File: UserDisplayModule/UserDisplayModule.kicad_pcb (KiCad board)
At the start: 2 copper layers, 0 parts

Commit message: doubled LEDs + started PCB
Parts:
- added C1: 10µ, Capacitor_SMD:C_0805_2012Metric, F.Cu at (60.5, 129.8)
- added D1: MAINS, LED_SMD:LED_0805_2012Metric, F.Cu at (89.2, 78.9)
- added D10: BAT3, LED_SMD:LED_0805_2012Metric, F.Cu at (93.7, 91.1)
- added D11: BAT8, LED_SMD:LED_0805_2012Metric, F.Cu at (100.0, 41.8)
- added D12: BAT1, LED_SMD:LED_0805_2012Metric, F.Cu at (100.0, 44.9)
- added D13: BAT7, LED_SMD:LED_0805_2012Metric, F.Cu at (100.0, 47.9)
- added D14: BAT1, LED_SMD:LED_0805_2012Metric, F.Cu at (100.0, 51.0)
- added D15: BAT6, LED_SMD:LED_0805_2012Metric, F.Cu at (104.5, 41.8)
- added D16: BAT1, LED_SMD:LED_0805_2012Metric, F.Cu at (104.5, 44.9)
- added D17: BAT5, LED_SMD:LED_0805_2012Metric, F.Cu at (104.5, 47.9)
- added D18: BAT1, LED_SMD:LED_0805_2012Metric, F.Cu at (104.5, 51.0)
- added D19: BAT4, LED_SMD:LED_0805_2012Metric, F.Cu at (108.9, 41.8)
- added D2: MAINS, LED_SMD:LED_0805_2012Metric, F.Cu at (89.2, 82.0)
- added D20: BAT1, LED_SMD:LED_0805_2012Metric, F.Cu at (108.9, 44.9)
- added D21: BAT3, LED_SMD:LED_0805_2012Metric, F.Cu at (108.9, 47.9)
- added D22: BAT1, LED_SMD:LED_0805_2012Metric, F.Cu at (108.9, 51.0)
- added D23: BAT2, LED_SMD:LED_0805_2012Metric, F.Cu at (113.4, 41.8)
- added D24: BAT1, LED_SMD:LED_0805_2012Metric, F.Cu at (113.4, 44.9)
- added D25: BAT1, LED_SMD:LED_0805_2012Metric, F.Cu at (113.4, 47.9)
- added D26: BAT1, LED_SMD:LED_0805_2012Metric, F.Cu at (113.4, 51.0)
- added D27: SEG7, LED_SMD:LED_0805_2012Metric, F.Cu at (208.0, 46.4)
- added D28: BAT1, LED_SMD:LED_0805_2012Metric, F.Cu at (208.0, 49.9)
- added D29: SEG6, LED_SMD:LED_0805_2012Metric, F.Cu at (205.1, 52.4)
- added D3: SOLAR, LED_SMD:LED_0805_2012Metric, F.Cu at (89.2, 85.0)
- added D30: BAT1, LED_SMD:LED_0805_2012Metric, F.Cu at (201.6, 52.4)
- added D31: SEG5, LED_SMD:LED_0805_2012Metric, F.Cu at (192.3, 52.4)
- added D32: BAT1, LED_SMD:LED_0805_2012Metric, F.Cu at (195.8, 52.4)
- added D33: SEG4, LED_SMD:LED_0805_2012Metric, F.Cu at (189.5, 46.4)
- added D34: BAT1, LED_SMD:LED_0805_2012Metric, F.Cu at (189.5, 49.9)
- added D35: SEG3, LED_SMD:LED_0805_2012Metric, F.Cu at (195.8, 43.9)
- added D36: BAT1, LED_SMD:LED_0805_2012Metric, F.Cu at (192.3, 43.9)
- added D37: SEG2, LED_SMD:LED_0805_2012Metric, F.Cu at (205.1, 43.9)
- added D38: BAT1, LED_SMD:LED_0805_2012Metric, F.Cu at (201.6, 43.9)
- added D39: SEG1, LED_SMD:LED_0805_2012Metric, F.Cu at (198.8, 46.4)
- added D4: BATTERY, LED_SMD:LED_0805_2012Metric, F.Cu at (89.2, 88.1)
- added D40: BAT1, LED_SMD:LED_0805_2012Metric, F.Cu at (198.8, 49.9)
- added D41: PTVS5V0Z1USK, Diode_SMD:Nexperia_DSN1608-2_1.6x0.8mm, F.Cu at (52.5, 147.3)
- added D42: COL2, LED_SMD:LED_0805_2012Metric, F.Cu at (98.1, 78.9)
- added D43: BAT3, LED_SMD:LED_0805_2012Metric, F.Cu at (98.1, 82.0)
- added D44: COL1, LED_SMD:LED_0805_2012Metric, F.Cu at (98.1, 85.0)
- added D45: BAT3, LED_SMD:LED_0805_2012Metric, F.Cu at (98.1, 88.1)
- added D46: SEG7, LED_SMD:LED_0805_2012Metric, F.Cu at (208.0, 70.2)
- added D47: BAT1, LED_SMD:LED_0805_2012Metric, F.Cu at (208.0, 73.8)
- added D48: SEG6, LED_SMD:LED_0805_2012Metric, F.Cu at (205.1, 76.3)
- added D49: BAT1, LED_SMD:LED_0805_2012Metric, F.Cu at (201.6, 76.3)
- added D5: BATTERY, LED_SMD:LED_0805_2012Metric, F.Cu at (89.2, 91.1)
- added D50: SEG5, LED_SMD:LED_0805_2012Metric, F.Cu at (192.3, 76.2)
- added D51: BAT1, LED_SMD:LED_0805_2012Metric, F.Cu at (195.8, 76.2)
- added D52: SEG4, LED_SMD:LED_0805_2012Metric, F.Cu at (189.5, 70.2)
- added D53: BAT1, LED_SMD:LED_0805_2012Metric, F.Cu at (189.5, 73.7)
- added D54: SEG3, LED_SMD:LED_0805_2012Metric, F.Cu at (195.8, 67.8)
- added D55: BAT1, LED_SMD:LED_0805_2012Metric, F.Cu at (192.3, 67.8)
- added D56: SEG2, LED_SMD:LED_0805_2012Metric, F.Cu at (205.1, 67.8)
- added D57: BAT1, LED_SMD:LED_0805_2012Metric, F.Cu at (201.6, 67.8)
- added D58: SEG1, LED_SMD:LED_0805_2012Metric, F.Cu at (198.8, 70.2)
- added D59: BAT1, LED_SMD:LED_0805_2012Metric, F.Cu at (198.8, 73.8)
- added D6: BAT7, LED_SMD:LED_0805_2012Metric, F.Cu at (93.7, 78.9)
- added D60: SEG7, LED_SMD:LED_0805_2012Metric, F.Cu at (208.0, 94.2)
- added D61: BAT1, LED_SMD:LED_0805_2012Metric, F.Cu at (208.0, 97.8)
- added D62: SEG6, LED_SMD:LED_0805_2012Metric, F.Cu at (205.1, 100.2)
- added D63: BAT1, LED_SMD:LED_0805_2012Metric, F.Cu at (201.6, 100.2)
- added D64: SEG5, LED_SMD:LED_0805_2012Metric, F.Cu at (192.3, 100.2)
- added D65: BAT1, LED_SMD:LED_0805_2012Metric, F.Cu at (195.8, 100.2)
- added D66: SEG4, LED_SMD:LED_0805_2012Metric, F.Cu at (189.5, 94.2)
- added D67: BAT1, LED_SMD:LED_0805_2012Metric, F.Cu at (189.5, 97.8)
- added D68: SEG3, LED_SMD:LED_0805_2012Metric, F.Cu at (195.8, 91.8)
- added D69: BAT1, LED_SMD:LED_0805_2012Metric, F.Cu at (192.3, 91.8)
- added D7: SYS WARN, LED_SMD:LED_0805_2012Metric, F.Cu at (93.7, 82.0)
- added D70: SEG2, LED_SMD:LED_0805_2012Metric, F.Cu at (205.1, 91.8)
- added D71: BAT1, LED_SMD:LED_0805_2012Metric, F.Cu at (201.6, 91.8)
- added D72: SEG1, LED_SMD:LED_0805_2012Metric, F.Cu at (198.8, 94.2)
- added D73: BAT1, LED_SMD:LED_0805_2012Metric, F.Cu at (198.8, 97.8)
- added D74: SEG7, LED_SMD:LED_0805_2012Metric, F.Cu at (207.7, 115.4)
- added D75: BAT1, LED_SMD:LED_0805_2012Metric, F.Cu at (207.7, 118.9)
- added D76: SEG6, LED_SMD:LED_0805_2012Metric, F.Cu at (204.8, 121.5)
- added D77: BAT1, LED_SMD:LED_0805_2012Metric, F.Cu at (201.2, 121.5)
- added D78: SEG5, LED_SMD:LED_0805_2012Metric, F.Cu at (192.0, 121.5)
- added D79: BAT1, LED_SMD:LED_0805_2012Metric, F.Cu at (195.5, 121.5)
- added D8: BAT5, LED_SMD:LED_0805_2012Metric, F.Cu at (93.7, 85.0)
- added D80: SEG4, LED_SMD:LED_0805_2012Metric, F.Cu at (189.2, 115.4)
- added D81: BAT1, LED_SMD:LED_0805_2012Metric, F.Cu at (189.2, 118.9)
- added D82: SEG3, LED_SMD:LED_0805_2012Metric, F.Cu at (195.5, 113.0)
- added D83: BAT1, LED_SMD:LED_0805_2012Metric, F.Cu at (192.0, 113.0)
- added D84: SEG2, LED_SMD:LED_0805_2012Metric, F.Cu at (204.8, 113.0)
- added D85: BAT1, LED_SMD:LED_0805_2012Metric, F.Cu at (201.3, 113.0)
- added D86: SEG1, LED_SMD:LED_0805_2012Metric, F.Cu at (198.4, 115.5)
- added D87: BAT1, LED_SMD:LED_0805_2012Metric, F.Cu at (198.4, 119.0)
- added D9: SYS FAIL, LED_SMD:LED_0805_2012Metric, F.Cu at (93.7, 88.1)
- added H1: MountingHole_Pad, MountingHole:MountingHole_3.2mm_M3_Pad, F.Cu at (32.5, 32.5)
- added H2: MountingHole_Pad, MountingHole:MountingHole_3.2mm_M3_Pad, F.Cu at (32.5, 156.5)
- added H3: MountingHole_Pad, MountingHole:MountingHole_3.2mm_M3_Pad, F.Cu at (220.5, 32.5)
- added H4: MountingHole_Pad, MountingHole:MountingHole_3.2mm_M3_Pad, F.Cu at (220.5, 156.5)
- added J1: RJ45_Shielded, Connector_RJ:RJ45_Shielded_EthernetJack, F.Cu at (48.7, 32.5)
- added R1: R_US, Resistor_SMD:R_0805_2012Metric, F.Cu at (84.8, 78.9)
- added R10: R_US, Resistor_SMD:R_0805_2012Metric, F.Cu at (85.0, 56.6)
- added R11: R_US, Resistor_SMD:R_0805_2012Metric, F.Cu at (85.0, 59.5)
- added R12: R_US, Resistor_SMD:R_0805_2012Metric, F.Cu at (85.0, 62.5)
- added R13: R_US, Resistor_SMD:R_0805_2012Metric, F.Cu at (179.1, 40.1)
- added R14: R_US, Resistor_SMD:R_0805_2012Metric, F.Cu at (179.1, 43.0)
- added R15: R_US, Resistor_SMD:R_0805_2012Metric, F.Cu at (179.1, 46.0)
- added R16: R_US, Resistor_SMD:R_0805_2012Metric, F.Cu at (179.1, 49.0)
- added R17: R_US, Resistor_SMD:R_0805_2012Metric, F.Cu at (179.1, 51.9)
- added R18: R_US, Resistor_SMD:R_0805_2012Metric, F.Cu at (179.1, 54.9)
- added R19: R_US, Resistor_SMD:R_0805_2012Metric, F.Cu at (179.1, 57.8)
- added R2: R_US, Resistor_SMD:R_0805_2012Metric, F.Cu at (84.8, 81.9)
- added R20: R_US, Resistor_SMD:R_0805_2012Metric, F.Cu at (84.8, 90.7)
- added R21: R_US, Resistor_SMD:R_0805_2012Metric, F.Cu at (84.8, 93.7)
- added R22: 16k, Resistor_SMD:R_0805_2012Metric, F.Cu at (56.1, 129.8)
- added R23: R_US, Resistor_SMD:R_0805_2012Metric, F.Cu at (84.8, 96.6)
- added R24: R_US, Resistor_SMD:R_0805_2012Metric, F.Cu at (178.7, 63.6)
- added R25: R_US, Resistor_SMD:R_0805_2012Metric, F.Cu at (178.7, 66.5)
- added R26: R_US, Resistor_SMD:R_0805_2012Metric, F.Cu at (178.7, 69.5)
- added R27: R_US, Resistor_SMD:R_0805_2012Metric, F.Cu at (178.7, 72.4)
- added R28: R_US, Resistor_SMD:R_0805_2012Metric, F.Cu at (178.7, 75.4)
- added R29: R_US, Resistor_SMD:R_0805_2012Metric, F.Cu at (178.7, 78.3)
- added R3: R_US, Resistor_SMD:R_0805_2012Metric, F.Cu at (84.8, 84.8)
- added R30: R_US, Resistor_SMD:R_0805_2012Metric, F.Cu at (178.7, 81.3)
- added R31: R_US, Resistor_SMD:R_0805_2012Metric, F.Cu at (178.9, 87.4)
- added R32: R_US, Resistor_SMD:R_0805_2012Metric, F.Cu at (178.9, 90.4)
- added R33: R_US, Resistor_SMD:R_0805_2012Metric, F.Cu at (178.9, 93.3)
- added R34: R_US, Resistor_SMD:R_0805_2012Metric, F.Cu at (178.9, 96.3)
- added R35: R_US, Resistor_SMD:R_0805_2012Metric, F.Cu at (178.9, 99.2)
- added R36: R_US, Resistor_SMD:R_0805_2012Metric, F.Cu at (178.9, 102.2)
- added R37: R_US, Resistor_SMD:R_0805_2012Metric, F.Cu at (178.9, 105.1)
- added R38: R_US, Resistor_SMD:R_0805_2012Metric, F.Cu at (178.9, 113.1)
- added R39: R_US, Resistor_SMD:R_0805_2012Metric, F.Cu at (178.9, 116.0)
- added R4: R_US, Resistor_SMD:R_0805_2012Metric, F.Cu at (84.8, 87.8)
- added R40: R_US, Resistor_SMD:R_0805_2012Metric, F.Cu at (178.9, 119.0)
- added R41: R_US, Resistor_SMD:R_0805_2012Metric, F.Cu at (178.9, 121.9)
- added R42: R_US, Resistor_SMD:R_0805_2012Metric, F.Cu at (178.9, 124.9)
- added R43: R_US, Resistor_SMD:R_0805_2012Metric, F.Cu at (178.9, 127.8)
- added R44: R_US, Resistor_SMD:R_0805_2012Metric, F.Cu at (178.9, 130.8)
- added R45: 1M, Resistor_SMD:R_0805_2012Metric, F.Cu at (38.4, 32.5)
- added R46: 1M, Resistor_SMD:R_0805_2012Metric, F.Cu at (38.5, 156.5)
- added R47: 1M, Resistor_SMD:R_0805_2012Metric, F.Cu at (214.5, 32.5)
- added R48: 1M, Resistor_SMD:R_0805_2012Metric, F.Cu at (214.4, 156.5)
- added R5: R_US, Resistor_SMD:R_0805_2012Metric, F.Cu at (85.0, 41.8)
- added R6: R_US, Resistor_SMD:R_0805_2012Metric, F.Cu at (85.0, 44.8)
- added R7: R_US, Resistor_SMD:R_0805_2012Metric, F.Cu at (85.0, 47.7)
- added R8: R_US, Resistor_SMD:R_0805_2012Metric, F.Cu at (85.0, 50.7)
- added R9: R_US, Resistor_SMD:R_0805_2012Metric, F.Cu at (85.0, 53.6)
- added RV1: 10K, Potentiometer_THT:Potentiometer_Rotary, F.Cu at (51.5, 141.5)
- added U1: 74HC595, ImportedFootprints:CD74HC595E, F.Cu at (81.1, 97.0)
- added U2: LM324, ImportedFootprints:LM324N, F.Cu at (54.5, 121.8)
- added U3: 74HC595, ImportedFootprints:CD74HC595E, F.Cu at (167.5, 63.5)
- added U4: 74HC595, ImportedFootprints:CD74HC595E, F.Cu at (167.5, 38.5)
- added U5: 74HC595, ImportedFootprints:CD74HC595E, F.Cu at (96.3, 59.9)
- added U6: 74HC595, ImportedFootprints:CD74HC595E, F.Cu at (167.6, 87.7)
- added U7: 74HC595, ImportedFootprints:CD74HC595E, F.Cu at (167.5, 111.3)
- added U8: LM7805_TO220, Package_TO_SOT_THT:TO-220-3_Vertical, F.Cu at (51.0, 53.4)
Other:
- board outline added: 203 x 139 mm

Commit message: started routing (help)
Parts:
- moved U1 110.0 mm to (183.7, 57.1)
- moved D45 103.9 mm to (200.0, 67.2)
- moved D44 103.7 mm to (199.9, 65.2), turned to 180 degrees
- moved R20 102.3 mm to (173.2, 39.3), turned to 180 degrees
- moved R4 99.6 mm to (173.2, 41.9), turned to 180 degrees
- moved R23 99.0 mm to (173.2, 52.0), turned to 180 degrees
- moved R3 97.2 mm to (173.2, 44.4), turned to 180 degrees
- moved R21 96.7 mm to (173.2, 54.6), turned to 180 degrees
- moved D43 95.5 mm to (192.5, 67.2)
- moved D42 95.3 mm to (192.5, 65.2), turned to 180 degrees
- moved R2 95.1 mm to (173.2, 47.0), turned to 180 degrees
- moved R1 93.2 mm to (173.2, 49.5), turned to 180 degrees
- moved D2 86.5 mm to (166.0, 42.0), turned to 90 degrees
- moved D1 83.3 mm to (163.9, 42.0), turned to -90 degrees
- moved D4 72.8 mm to (145.6, 42.0), turned to 90 degrees
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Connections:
- R1 pad 1: Net-(U1-QH) -> Net-(U1-QF)
- R2 pad 1: Net-(U1-QG) -> Net-(U1-QE)
- R20 pad 1: Net-(U1-QD) -> Net-(U1-QB)
- R21 pad 1: Net-(U1-QC) -> Net-(U1-QH)
- R23 pad 1: Net-(U1-QB) -> Net-(U1-QG)
- R3 pad 1: Net-(U1-QF) -> Net-(U1-QD)
- R4 pad 1: Net-(U1-QE) -> Net-(U1-QC)
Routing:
- net Net-(D25-A): track 0.00 -> 34.8 mm
- net Net-(D27-A): track 0.00 -> 30.1 mm
- net Net-(D29-A): track 0.00 -> 30.0 mm
- net Net-(D37-A): track 0.00 -> 24.7 mm, vias 0 -> 2
- net Net-(D39-A): track 0.00 -> 17.8 mm, vias 0 -> 2
- net Net-(D31-A): track 0.00 -> 17.5 mm
- net Net-(D35-A): track 0.00 -> 17.3 mm, vias 0 -> 2
- net Net-(D23-A): track 0.00 -> 16.6 mm
- net Net-(D21-A): track 0.00 -> 16.0 mm
- net Net-(D19-A): track 0.00 -> 15.5 mm
- net Net-(D17-A): track 0.00 -> 14.9 mm
- net Net-(D15-A): track 0.00 -> 14.3 mm
- net Net-(D13-A): track 0.00 -> 13.7 mm
- net Net-(D11-A): track 0.00 -> 13.7 mm
- net (no net): track 0.00 -> 13.6 mm, vias 0 -> 2
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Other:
- board size 203 x 139 mm -> 196.6 x 93 mm
- board text added: "AC MAINS"
- board text added: "BATTERY"
- board text added: "HARDWARE"
- board text added: "POWER"
- board text added: "SOLAR"
- board text added: "SYSTEM FAILURE"
- board text added: "SYSTEM WARNING"

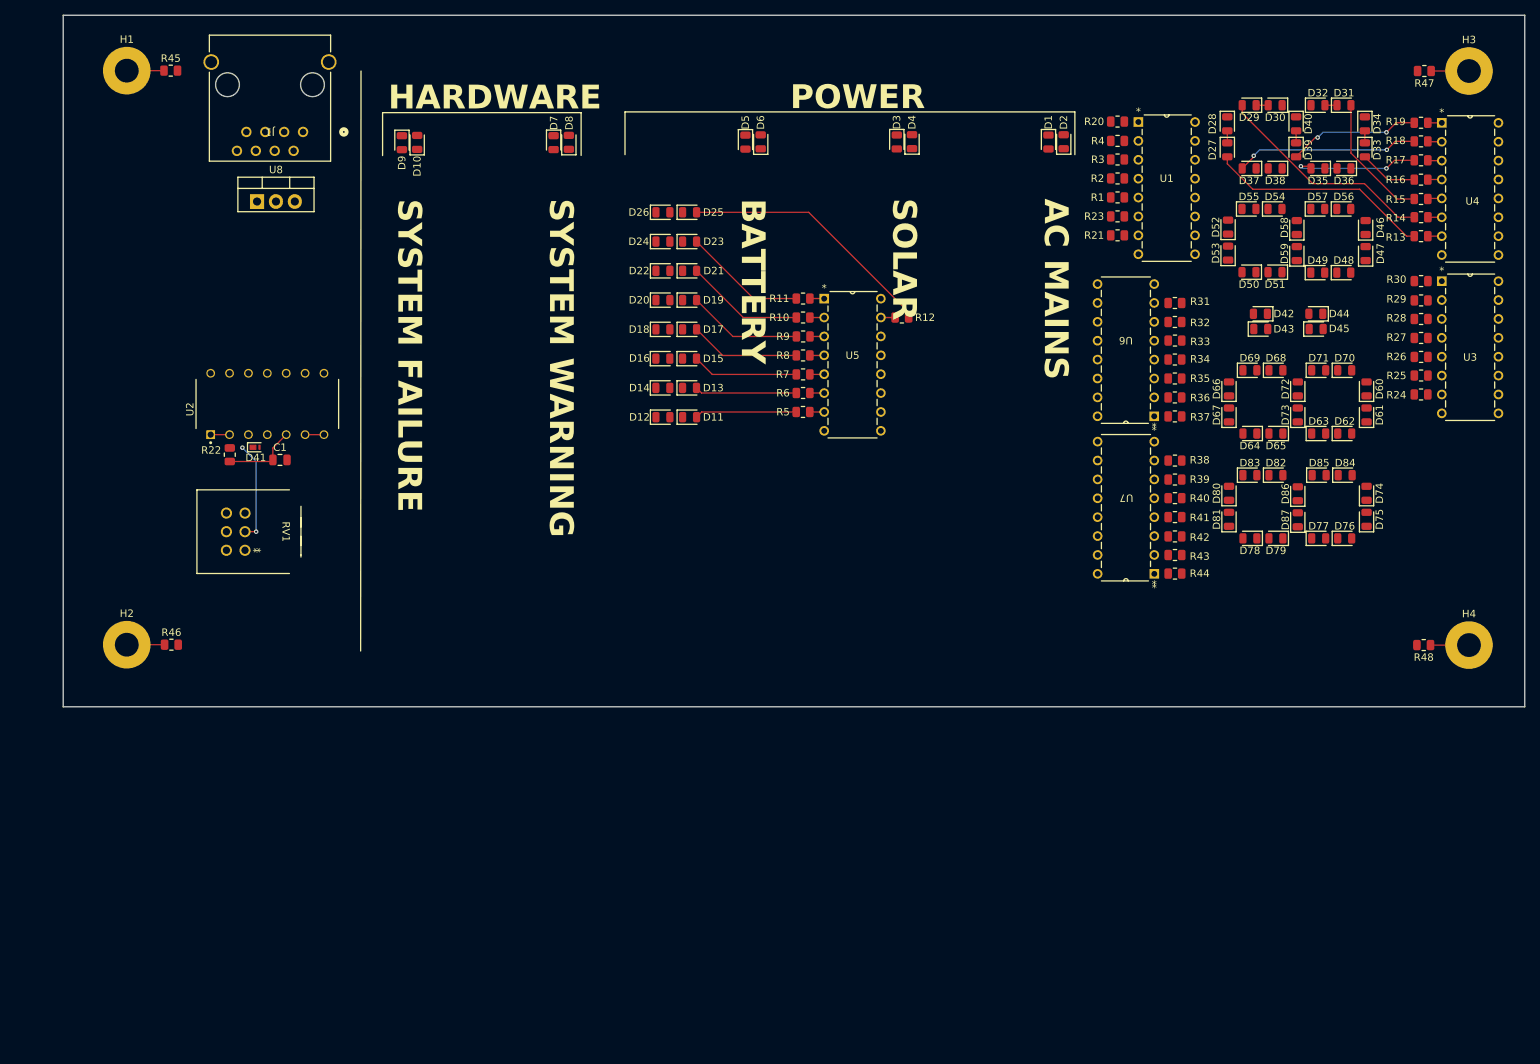
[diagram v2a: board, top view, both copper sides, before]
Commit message: finished routing pcb (minus ground pour)
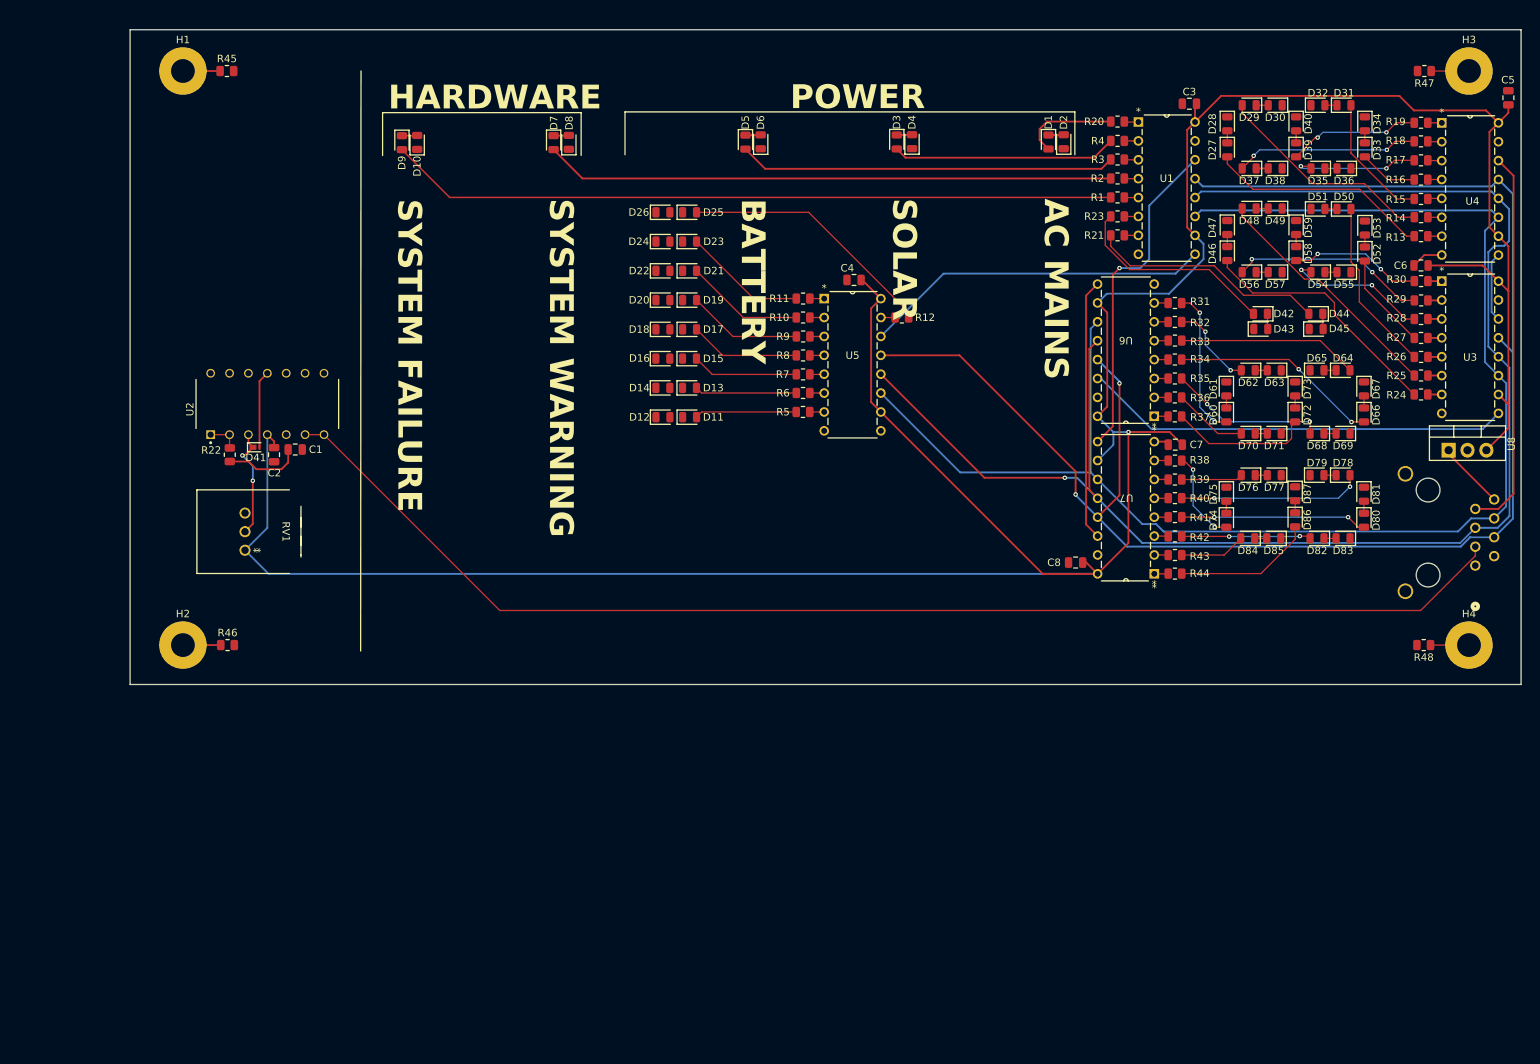
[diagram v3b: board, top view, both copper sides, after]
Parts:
- added C2: C, Capacitor_SMD:C_0805_2012Metric, F.Cu at (59.8, 84.1)
- added C3: C, Capacitor_SMD:C_0805_2012Metric, F.Cu at (182.9, 36.9)
- added C4: C, Capacitor_SMD:C_0805_2012Metric, F.Cu at (137.8, 60.6)
- added C5: C, Capacitor_SMD:C_0805_2012Metric, F.Cu at (225.8, 36.1)
- added C6: C, Capacitor_SMD:C_0805_2012Metric, F.Cu at (214.1, 58.6)
- added C7: C, Capacitor_SMD:C_0805_2012Metric, F.Cu at (181.0, 82.8)
- added C8: C, Capacitor_SMD:C_0805_2012Metric, F.Cu at (167.6, 98.6)
- J1: moved to B.Cu
- moved J1 168.1 mm to (221.3, 99.0), turned to 90 degrees
- moved U8 163.7 mm to (217.8, 83.5)
- moved D74 19.2 mm to (187.9, 92.9), turned to -90 degrees
- moved D60 19.2 mm to (187.9, 78.8), turned to -90 degrees
- moved D61 19.2 mm to (187.9, 75.2), turned to -90 degrees
- moved D75 19.1 mm to (187.9, 89.4), turned to -90 degrees
- moved D46 18.9 mm to (188.0, 57.0), turned to -90 degrees
- moved D47 18.9 mm to (188.0, 53.5), turned to -90 degrees
- moved D52 18.8 mm to (206.5, 57.1), turned to -90 degrees
- moved D53 18.7 mm to (206.5, 53.6), turned to -90 degrees
- moved D80 18.5 mm to (206.4, 92.9), turned to -90 degrees
- moved D66 18.5 mm to (206.4, 78.8), turned to -90 degrees
- moved D67 18.5 mm to (206.4, 75.2), turned to -90 degrees
- moved D81 18.5 mm to (206.4, 89.4), turned to -90 degrees
- moved D84 15.6 mm to (190.8, 95.3), turned to 180 degrees
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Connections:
- R1 pad 2: Net-(D1-A) -> Net-(D9-A)
- R2 pad 2: Net-(D3-A) -> Net-(D7-A)
- R20 pad 2: Net-(D9-A) -> Net-(D1-A)
- R21 pad 2: Net-(D42-A) -> Net-(D44-A)
- R23 pad 2: Net-(D44-A) -> Net-(D42-A)
- R4 pad 2: Net-(D7-A) -> Net-(D3-A)
- U1 pad 14: DATA -> /7-Segment Display 4/DATA_OUT
- U4 pad 14: /7-Segment Display 1/DATA_IN -> DATA
- U5 pad 9: /7-Segment Display 1/DATA_IN -> /Battery LEDs/DATA_OUT
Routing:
- net 5V: track 0.00 -> 397.7 mm, vias 0 -> 1
- net OE: track 0.00 -> 213.5 mm, vias 0 -> 2
- net RCLK: track 0.00 -> 205.5 mm, vias 0 -> 1
- net SRCLK: track 0.00 -> 196.2 mm
- net /Brightness Dial/Brightness: track 2.54 -> 171.4 mm
- net Net-(D9-A): track 0.00 -> 98.0 mm
- net Net-(D7-A): track 0.00 -> 76.5 mm
- net /7-Segment Display 2/DATA_OUT: track 0.00 -> 57.6 mm
- net DATA: track 0.00 -> 51.6 mm
- net Net-(D5-A): track 0.00 -> 50.7 mm
- net /Battery LEDs/DATA_IN: track 0.00 -> 46.8 mm
- net /7-Segment Display 4/DATA_OUT: track 0.00 -> 45.0 mm, vias 0 -> 1
- net /7-Segment Display 3/DATA_OUT: track 0.00 -> 35.2 mm
- net Net-(D46-A): track 0.00 -> 34.1 mm
- net Net-(D48-A): track 0.00 -> 33.1 mm
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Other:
- board size 196.6 x 93 mm -> 187.1 x 88 mm

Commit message: added ground pour + finished routing
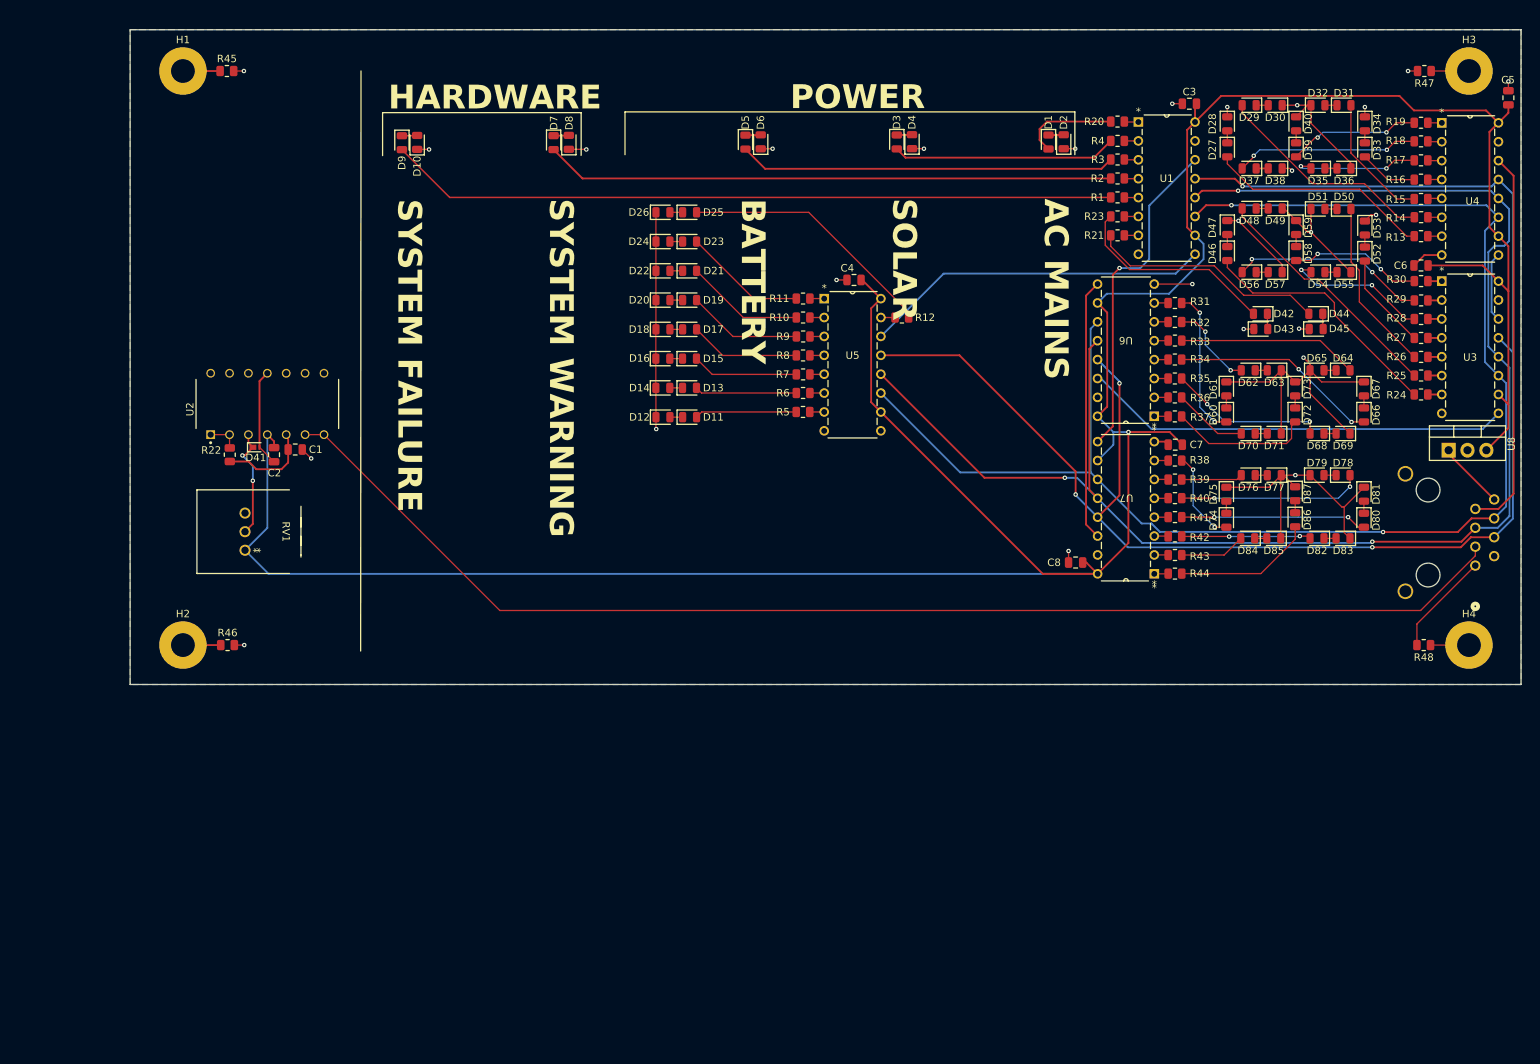
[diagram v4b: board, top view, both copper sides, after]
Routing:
- net GND: track 16.8 -> 220.5 mm, vias 0 -> 26
- net Net-(U2B-+): track 10.4 -> 12.5 mm
- net Net-(D25-K): track 0.00 -> 1.71 mm
- net Net-(D23-K): track 0.00 -> 1.71 mm
- net Net-(D21-K): track 0.00 -> 1.71 mm
- net Net-(D19-K): track 0.00 -> 1.71 mm
- net Net-(D17-K): track 0.00 -> 1.71 mm
- net Net-(D11-K): track 0.00 -> 1.71 mm
- net Net-(D15-K): track 0.00 -> 1.71 mm
- net Net-(D13-K): track 0.00 -> 1.71 mm
- net Net-(D35-K): track 0.00 -> 1.62 mm
- net SRCLK: track 196.2 -> 196.8 mm, vias 0 -> 2
- net RCLK: track 205.5 -> 205.6 mm, vias 1 -> 3
- net OE: vias 2 -> 4
- added copper zone on B.Cu, net GND
